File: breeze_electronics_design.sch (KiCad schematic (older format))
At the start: 100 parts, among them M1 Motor, M2 Motor, M3 Motor, M4 Motor, Q2 SI2303, Q3 SI2303, Q4 SI2303, Q5 SI2303, U10 MPU6050, U11 MS5611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

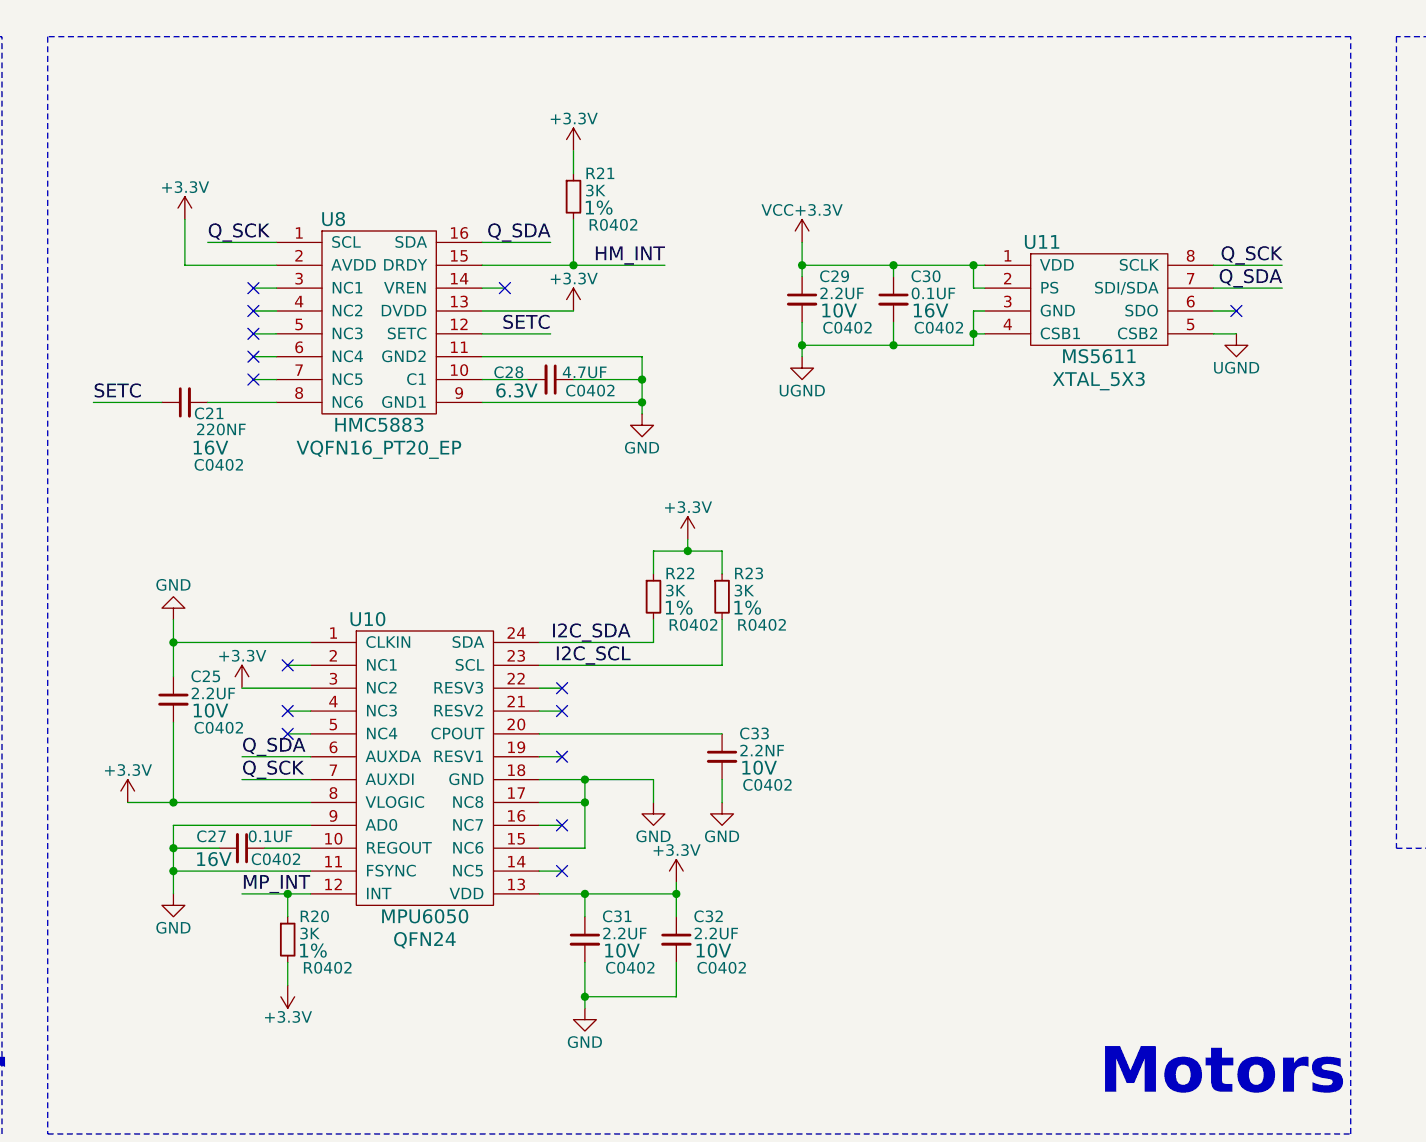
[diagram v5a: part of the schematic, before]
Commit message: Modify the schematic of Sensors
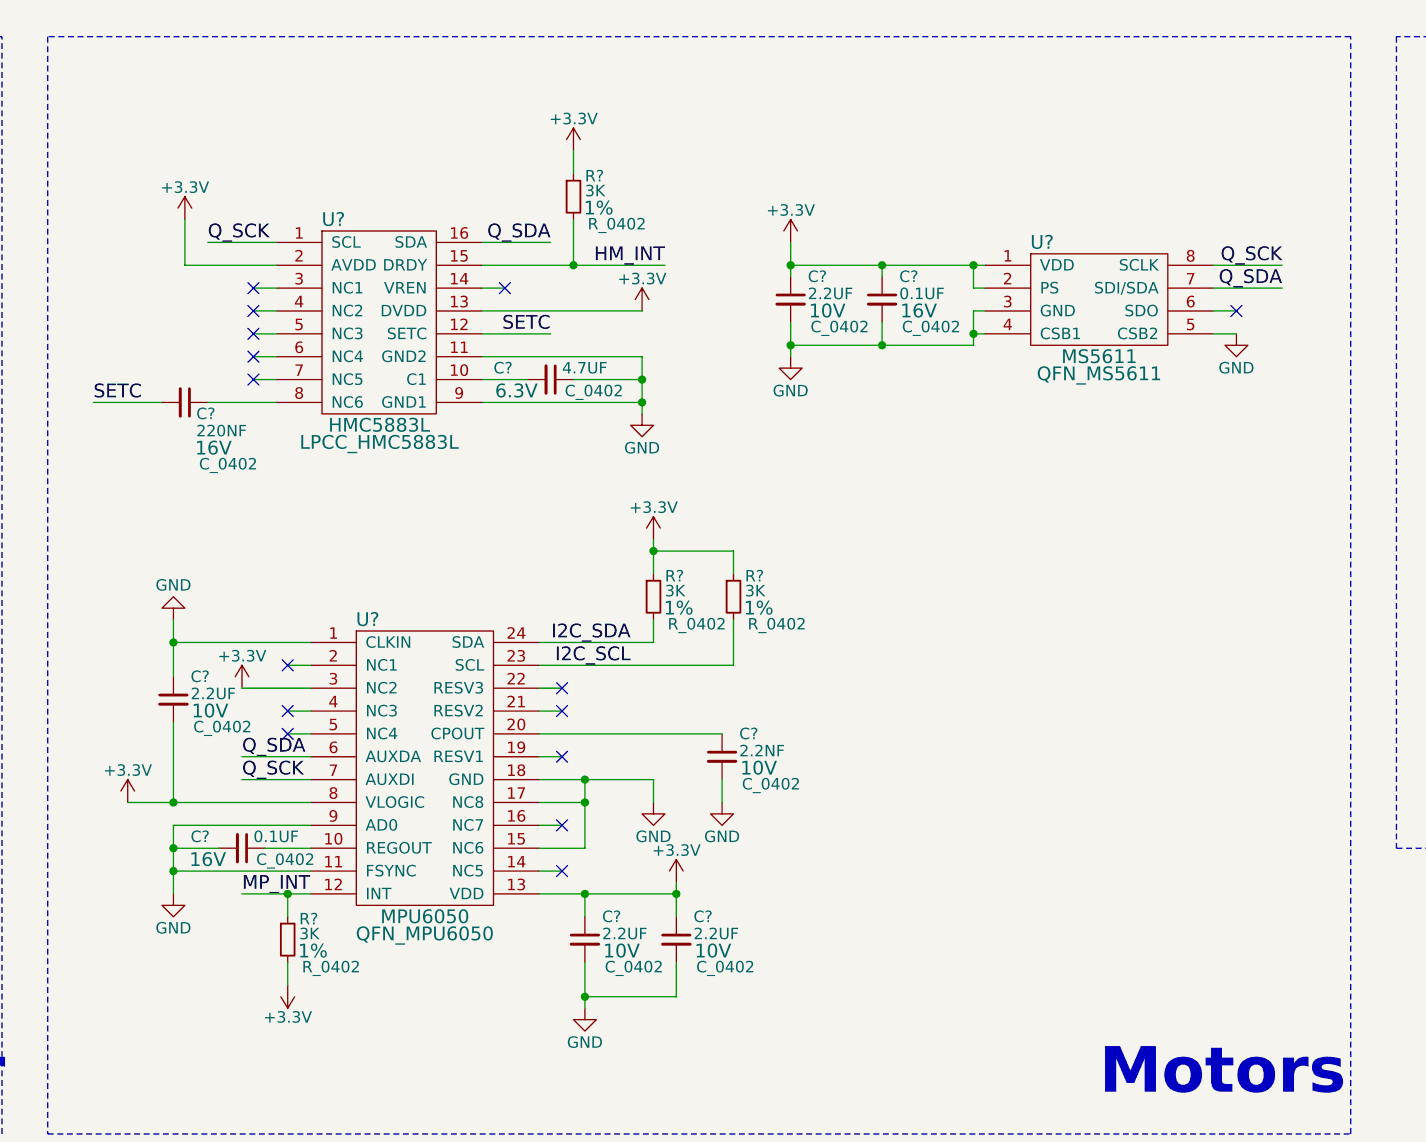
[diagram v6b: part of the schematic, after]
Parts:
- removed C21: 220NF, C0402, symbol Capacitance
- removed C25, C29, C31, C32: 2.2UF, C0402, symbol Capacitance
- removed C27, C30: 0.1UF, C0402, symbol Capacitance
- removed C28: 4.7UF, C0402, symbol Capacitance
- removed C33: 2.2NF, C0402, symbol Capacitance
- removed R20, R21, R22, R23: 3K, R0402, symbol Resistor
- removed U10: MPU6050, QFN24, symbol MPU6050
- removed U11: MS5611, XTAL_5X3, symbol MS5611
- removed U8: HMC5883, VQFN16_PT20_EP, symbol MHC5883
- added C?: 220NF, C_0402, symbol Capacitance
- added C?: 4.7UF, C_0402, symbol Capacitance
- added C? (x4): 2.2UF, C_0402, symbol Capacitance
- added C? (x2): 0.1UF, C_0402, symbol Capacitance
- added C?: 2.2NF, C_0402, symbol Capacitance
- added R? (x4): 3K, R_0402, symbol Resistor
- added U?: HMC5883L, LPCC_HMC5883L, symbol HMC5883L
- added U?: MS5611, QFN_MS5611, symbol MS5611
- added U?: MPU6050, QFN_MPU6050, symbol MPU6050
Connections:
- net HM_INT: now also R?.2, U?.15 (DRDY)
- net I2C_SCL: now also R?.2, U?.23 (SCL)
- net I2C_SDA: now also R?.2, U?.24 (SDA)
- net MP_INT: now also R?.1, U?.12 (INT)
- net Q_SCK: now also U?.1 (SCL), U?.7 (AUXDI), U?.8 (SCLK)
- net Q_SDA: now also U?.16 (SDA), U?.6 (AUXDA), U?.7 (SDI/SDA)
- net SETC: now also C?.2, U?.12 (SETC)
- new net: C?.2, U?.10 (C1)
- new net: C?.1, U?.11 (GND2), U?.9 (GND1)
- new net: C?.1, U?.8 (NC6)
- new net: C?.1, C?.1, U?.1 (VDD), U?.2 (PS)
- new net: C?.2, C?.2, U?.3 (GND), U?.4 (CSB1)
- new net: R?.1, R?.1
- new net: C?.1, U?.20 (CPOUT)
- new net: C?.1, C?.1, U?.13 (VDD)
- new net: C?.2, C?.2
- new net: C?.1, U?.1 (CLKIN)
- new net: C?.1, U?.10 (REGOUT)
- new net: C?.2, U?.11 (FSYNC), U?.9 (AD0)
- new net: U?.15 (NC6), U?.17 (NC8), U?.18 (GND)
- new net: C?.2, U?.8 (VLOGIC)

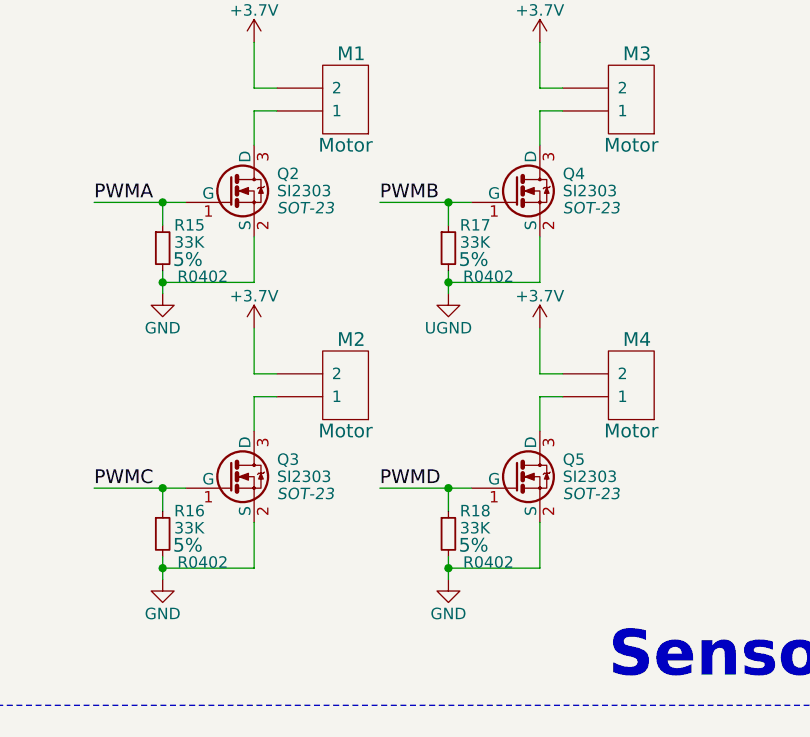
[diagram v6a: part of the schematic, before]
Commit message: Modify the schematic of Motors
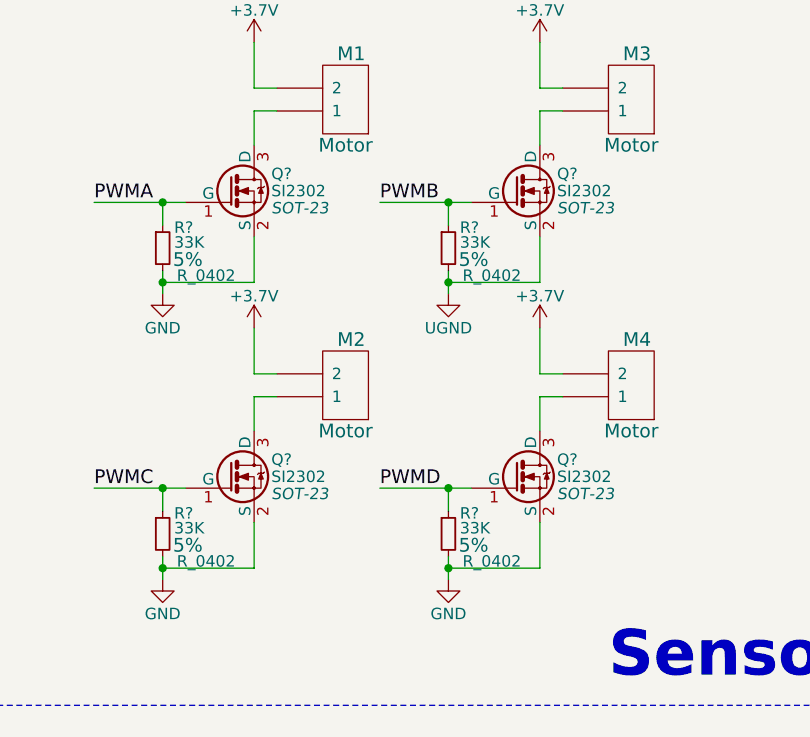
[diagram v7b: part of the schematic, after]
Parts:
- removed Q2, Q3, Q4, Q5: SI2303, SOT-23, symbol Mosfet
- removed R15, R16, R17, R18: 33K, R0402, symbol Resistor
- added Q? (x4): SI2302, SOT-23, symbol Mosfet
- added R? (x4): 33K, R_0402, symbol Resistor
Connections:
- net PWMA: now also Q?.1 (G), R?.1
- net PWMB: now also Q?.1 (G), R?.1
- net PWMC: now also Q?.1 (G), R?.1
- net PWMD: now also Q?.1 (G), R?.1
- net at M1.1: now also Q?.3 (D)
- net at M3.1: now also Q?.3 (D)
- net at M2.1: now also Q?.3 (D)
- net at M4.1: now also Q?.3 (D)
- new net: Q?.2 (S), R?.2 (x4)
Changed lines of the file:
@@
 	-1   0    0    1
 $EndComp
-$Comp
-L Mosfet Q2
-U 1 1 57B57475
-P 13100 7600
-F 0 "Q2" H 13250 7675 50  0000 L CNN
-F 1 "SI2303" H 13250 7600 50  0000 L CNN
-F 2 "SOT-23" H 13250 7525 50  0000 L CIN
-F 3 "" H 13050 7600 50  0000 L CNN
-	1    13100 7600
-	1    0    0    -1
-$EndComp
 Text Label 12450 7650 0    60   ~ 0
 PWMA
@@
 	-1   0    0    1
 $EndComp
-$Comp
-L Mosfet Q4
-U 1 1 57B5A57A
-P 14350 7600
-F 0 "Q4" H 14500 7675 50  0000 L CNN
-F 1 "SI2303" H 14500 7600 50  0000 L CNN
-F 2 "SOT-23" H 14500 7525 50  0000 L CIN
-F 3 "" H 14300 7600 50  0000 L CNN
-	1    14350 7600
-	1    0    0    -1
-$EndComp
 Text Label 13700 7650 0    60   ~ 0
 PWMB
@@
 	-1   0    0    1
 $EndComp
-$Comp
-L Mosfet Q3
-U 1 1 57B5B003
-P 13100 8850
-F 0 "Q3" H 13250 8925 50  0000 L CNN
-F 1 "SI2303" H 13250 8850 50  0000 L CNN
-F 2 "SOT-23" H 13250 8775 50  0000 L CIN
-F 3 "" H 13050 8850 50  0000 L CNN
-	1    13100 8850
-	1    0    0    -1
-$EndComp
 Text Label 12450 8900 0    60   ~ 0
 PWMC
@@
 	-1   0    0    1
 $EndComp
-$Comp
-L Mosfet Q5
-U 1 1 57B5B276
-P 14350 8850
-F 0 "Q5" H 14500 8925 50  0000 L CNN
-F 1 "SI2303" H 14500 8850 50  0000 L CNN
-F 2 "SOT-23" H 14500 8775 50  0000 L CIN
-F 3 "" H 14300 8850 50  0000 L CNN
-	1    14350 8850
-	1    0    0    -1
-$EndComp
 Text Label 13700 8900 0    60   ~ 0
 PWMD
@@
 	1    0    0    -1
 $EndComp
-$Comp
-L Resistor R15
-U 1 1 57BC2E8C
-P 12750 7850
-F 0 "R15" H 12800 7950 50  0000 L CNN
-F 1 "33K" H 12800 7875 50  0000 L CNN
-F 2 "R0402" H 12925 7725 50  0000 C CNN
-F 3 "" H 12750 7850 50  0000 C CNN
-F 4 "5%" H 12860 7800 60  0000 C CNN "Accuracy"
-	1    12750 7850
-	1    0    0    -1
-$EndComp
-$Comp
-L Resistor R17
-U 1 1 57BC3A5A
-P 14000 7850
-F 0 "R17" H 14050 7950 50  0000 L CNN
-F 1 "33K" H 14050 7875 50  0000 L CNN
-F 2 "R0402" H 14175 7725 50  0000 C CNN
-F 3 "" H 14000 7850 50  0000 C CNN
-F 4 "5%" H 14110 7800 60  0000 C CNN "Accuracy"
-	1    14000 7850
-	1    0    0    -1
-$EndComp
-$Comp
-L Resistor R16
-U 1 1 57BC450F
-P 12750 9100
-F 0 "R16" H 12800 9200 50  0000 L CNN
-F 1 "33K" H 12800 9125 50  0000 L CNN
-F 2 "R0402" H 12925 8975 50  0000 C CNN
-F 3 "" H 12750 9100 50  0000 C CNN
-F 4 "5%" H 12860 9050 60  0000 C CNN "Accuracy"
-	1    12750 9100
-	1    0    0    -1
-$EndComp
-$Comp
-L Resistor R18
-U 1 1 57BC55AF
-P 14000 9100
-F 0 "R18" H 14050 9200 50  0000 L CNN
-F 1 "33K" H 14050 9125 50  0000 L CNN
-F 2 "R0402" H 14175 8975 50  0000 C CNN
-F 3 "" H 14000 9100 50  0000 C CNN
-F 4 "5%" H 14110 9050 60  0000 C CNN "Accuracy"
-	1    14000 9100
-	1    0    0    -1
-$EndComp
 Text Notes 14700 9750 0    200  ~ 40
 Sensors
@@
 	1    0    0    -1
 $EndComp
+$Comp
+L Resistor R?
+U 1 1 57C365C5
+P 12750 7850
+F 0 "R?" H 12800 7940 50  0000 L CNN
+F 1 "33K" H 12800 7875 50  0000 L CNN
+F 2 "R_0402" H 12940 7730 50  0000 C CNN
+F 3 "" H 12750 7850 50  0000 C CNN
+F 4 "5%" H 12860 7800 60  0000 C CNN "Accuracy"
+	1    12750 7850
+	1    0    0    -1
+$EndComp
+$Comp
+L Resistor R?
+U 1 1 57C36E16
+P 14000 7850
+F 0 "R?" H 14050 7940 50  0000 L CNN
+F 1 "33K" H 14050 7875 50  0000 L CNN
+F 2 "R_0402" H 14190 7730 50  0000 C CNN
+F 3 "" H 14000 7850 50  0000 C CNN
+F 4 "5%" H 14110 7800 60  0000 C CNN "Accuracy"
+	1    14000 7850
+	1    0    0    -1
+$EndComp
+$Comp
+L Resistor R?
+U 1 1 57C379F1
+P 12750 9100
+F 0 "R?" H 12800 9190 50  0000 L CNN
+F 1 "33K" H 12800 9125 50  0000 L CNN
+F 2 "R_0402" H 12940 8980 50  0000 C CNN
+F 3 "" H 12750 9100 50  0000 C CNN
+F 4 "5%" H 12860 9050 60  0000 C CNN "Accuracy"
+	1    12750 9100
+	1    0    0    -1
+$EndComp
+$Comp
+L Resistor R?
+U 1 1 57C3830A
+P 14000 9100
+F 0 "R?" H 14050 9190 50  0000 L CNN
+F 1 "33K" H 14050 9125 50  0000 L CNN
+F 2 "R_0402" H 14190 8980 50  0000 C CNN
+F 3 "" H 14000 9100 50  0000 C CNN
+F 4 "5%" H 14110 9050 60  0000 C CNN "Accuracy"
+	1    14000 9100
+	1    0    0    -1
+$EndComp
+$Comp
+L Mosfet Q?
+U 1 1 57C39446
+P 13100 7600
+F 0 "Q?" H 13225 7675 50  0000 L CNN
+F 1 "SI2302" H 13225 7600 50  0000 L CNN
+F 2 "SOT-23" H 13225 7525 50  0000 L CIN
+F 3 "" H 13050 7600 50  0000 L CNN
+	1    13100 7600
+	1    0    0    -1
+$EndComp
+$Comp
+L Mosfet Q?
+U 1 1 57C39B5B
+P 14350 7600
+F 0 "Q?" H 14475 7675 50  0000 L CNN
+F 1 "SI2302" H 14475 7600 50  0000 L CNN
+F 2 "SOT-23" H 14475 7525 50  0000 L CIN
+F 3 "" H 14300 7600 50  0000 L CNN
+	1    14350 7600
+	1    0    0    -1
+$EndComp
+$Comp
+L Mosfet Q?
+U 1 1 57C3A4CD
+P 13100 8850
+F 0 "Q?" H 13225 8925 50  0000 L CNN
+F 1 "SI2302" H 13225 8850 50  0000 L CNN
+F 2 "SOT-23" H 13225 8775 50  0000 L CIN
+F 3 "" H 13050 8850 50  0000 L CNN
+	1    13100 8850
+	1    0    0    -1
+$EndComp
+$Comp
+L Mosfet Q?
+U 1 1 57C3AD77
+P 14350 8850
+F 0 "Q?" H 14475 8925 50  0000 L CNN
+F 1 "SI2302" H 14475 8850 50  0000 L CNN
+F 2 "SOT-23" H 14475 8775 50  0000 L CIN
+F 3 "" H 14300 8850 50  0000 L CNN
+	1    14350 8850
+	1    0    0    -1
+$EndComp
